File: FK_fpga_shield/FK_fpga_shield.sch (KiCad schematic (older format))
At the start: 137 parts, among them J0 USB_B_Mini, J1 molex-51382-0400-microclasp, J10 molex-51382-0400-microclasp, J11 molex-51382-0400-microclasp, J12 molex-51382-0400-microclasp, J13 molex-51382-0400-microclasp, J14 molex-51382-0400-microclasp, J15 molex-51382-0400-microclasp, J16 molex-51382-0400-microclasp, J17 molex-51382-0400-microclasp, J18 molex-51382-0400-microclasp, J19 molex-51382-0400-microclasp, J2 molex-51382-0400-microclasp, J20 molex-51382-0400-microclasp, J21 molex-51382-0400-microclasp, J22 molex-51382-0400-microclasp, J23 molex-51382-0400-microclasp, J24 molex-51382-0400-microclasp, J25 molex-51382-0400-microclasp, J26 molex-51382-0400-microclasp, J27 molex-51382-0400-microclasp, J28 molex-51382-0400-microclasp, J29 molex-51382-0400-microclasp, J3 molex-51382-0400-microclasp, J30 molex-51382-0400-microclasp, J31 molex-51382-0400-microclasp, J32 molex-51382-0400-microclasp, J33 molex-51382-0400-microclasp, J34 molex-51382-0400-microclasp, J35 molex-51382-0400-microclasp, J4 molex-51382-0400-microclasp, J5 molex-51382-0400-microclasp, J6 molex-51382-0400-microclasp, J7 molex-51382-0400-microclasp, J8 molex-51382-0400-microclasp, J9 molex-51382-0400-microclasp, U1 FT232RL, U2 nvt2010pw, U3 nvt2010pw, U4 nvt2010pw, U5 nvt2010pw, U6 nvt2010pw, U7 nvt2010pw, U8 nvt2010pw

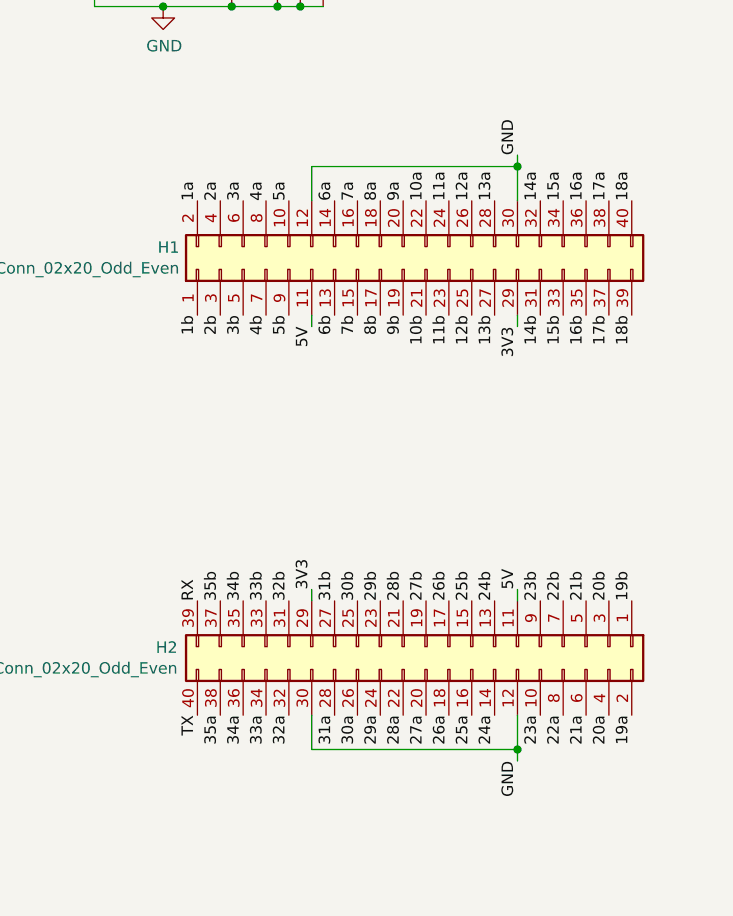
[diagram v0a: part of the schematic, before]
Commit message: levelshifter to fpga signals routed
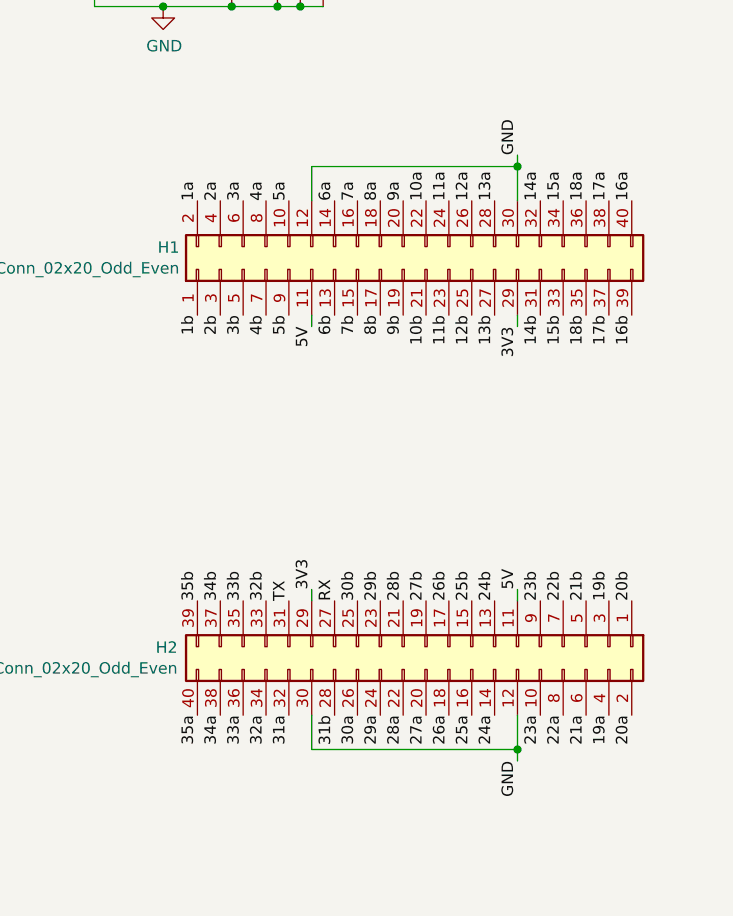
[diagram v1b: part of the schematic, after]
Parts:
- gave numbers to parts that had none: 1
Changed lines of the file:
@@
 	1    0    0    -1
 $EndComp
-Text Label 12950 6450 1    50   ~ 0
+Text Label 13550 6450 1    50   ~ 0
 RX
-Text Label 12950 6950 3    50   ~ 0
+Text Label 13350 6450 1    50   ~ 0
 TX
 Text Label 3550 2050 0    50   ~ 0
@@
 Text Label 14550 4700 1    50   ~ 0
 15a
-Text Label 14650 5200 3    50   ~ 0
+Text Label 14850 5200 3    50   ~ 0
 16b
-Text Label 14650 4700 1    50   ~ 0
+Text Label 14850 4700 1    50   ~ 0
 16a
 Text Label 14750 5200 3    50   ~ 0
@@
 Text Label 14750 4700 1    50   ~ 0
 17a
-Text Label 14850 5200 3    50   ~ 0
+Text Label 14650 5200 3    50   ~ 0
 18b
-Text Label 14850 4700 1    50   ~ 0
+Text Label 14650 4700 1    50   ~ 0
 18a
+Text Label 14750 6450 1    50   ~ 0
+19b
+Text Label 14750 6950 3    50   ~ 0
+19a
 Text Label 14850 6450 1    50   ~ 0
-19b
+20b
 Text Label 14850 6950 3    50   ~ 0
-19a
-Text Label 14750 6450 1    50   ~ 0
-20b
-Text Label 14750 6950 3    50   ~ 0
 20a
 Text Label 14650 6450 1    50   ~ 0
@@
 Text Label 14050 6450 1    50   ~ 0
 26b
-Text Label 13550 6450 1    50   ~ 0
+Text Label 13550 6950 3    50   ~ 0
 31b
-Text Label 13550 6950 3    50   ~ 0
+Text Label 13350 6950 3    50   ~ 0
 31a
-Text Label 13350 6450 1    50   ~ 0
+Text Label 13250 6450 1    50   ~ 0
 32b
-Text Label 13350 6950 3    50   ~ 0
+Text Label 13250 6950 3    50   ~ 0
 32a
-Text Label 13250 6450 1    50   ~ 0
+Text Label 13150 6450 1    50   ~ 0
 33b
-Text Label 13250 6950 3    50   ~ 0
+Text Label 13150 6950 3    50   ~ 0
 33a
-Text Label 13150 6450 1    50   ~ 0
-34b
-Text Label 13150 6950 3    50   ~ 0
-34a
-Text Label 13050 6450 1    50   ~ 0
-35b
-Text Label 13050 6950 3    50   ~ 0
-35a
 $Comp
-L Connector:Barrel_Jack J?
+L Connector:Barrel_Jack J36
 U 1 1 61D44947
 P 10300 6600
-F 0 "J?" H 10357 6925 50  0000 C CNN
+F 0 "J36" H 10357 6925 50  0000 C CNN
 F 1 "Barrel_Jack" H 10357 6834 50  0000 C CNN
 F 2 "" H 10350 6560 50  0001 C CNN
@@
 $EndComp
 $Comp
-L power:GND #PWR?
+L power:GND #PWR0112
 U 1 1 61D45B36
 P 10750 6700
-F 0 "#PWR?" H 10750 6450 50  0001 C CNN
+F 0 "#PWR0112" H 10750 6450 50  0001 C CNN
 F 1 "GND" H 10755 6527 50  0000 C CNN
 F 2 "" H 10750 6700 50  0001 C CNN
@@
 Wire Wire Line
 	10600 6500 10750 6500
+Text Label 12950 6950 3    50   ~ 0
+35a
+Text Label 13050 6950 3    50   ~ 0
+34a
+Text Label 12950 6450 1    50   ~ 0
+35b
+Text Label 13050 6450 1    50   ~ 0
+34b
 $EndSCHEMATC

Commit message: wip routing (usb done (?))
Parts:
- added C12, C13: dnp, Capacitor_SMD:C_0805_2012Metric_Pad1.15x1.40mm_HandSolder, symbol Device:C_Small
- added Y1: DNP_(12MHz), Crystal:Crystal_SMD_HC49-SD, symbol Device:Crystal
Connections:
- wire segments 541 -> 552
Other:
- note added: "External oscillator not reqired\nper datasheet when 5V powered.\nFootprint added anyway just in case."
- note removed: "External oscillator not reqired\nper datasheet when 5V powered.\n"
- moved on the sheet: C1, C2, C3, C4, J0, R1, R2, U1

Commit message: decouple 3V3 references just in case
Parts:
- removed J36: Barrel_Jack, symbol Connector:Barrel_Jack
- added C? (x7): 100n, Capacitor_SMD:C_0805_2012Metric_Pad1.15x1.40mm_HandSolder, symbol Device:C_Small
- added J36: Barrel_Jack_MountingPin, Connector_BarrelJack:BarrelJack_CUI_PJ-063AH_Horizontal, symbol Connector:Barrel_Jack_MountingPin
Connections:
- wire segments 552 -> 573
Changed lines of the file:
@@
 	1    0    0    -1
 $EndComp
-Wire Wire Line
-	3600 10450 3450 10450
 Text Label 3600 10550 3    50   ~ 0
 3V3
@@
 33a
 $Comp
-L Connector:Barrel_Jack J36
-U 1 1 61D44947
-P 10300 6600
-F 0 "J36" H 10357 6925 50  0000 C CNN
-F 1 "Barrel_Jack" H 10357 6834 50  0000 C CNN
-F 2 "" H 10350 6560 50  0001 C CNN
-F 3 "~" H 10350 6560 50  0001 C CNN
-	1    10300 6600
-	1    0    0    -1
-$EndComp
-$Comp
 L power:GND #PWR0112
 U 1 1 61D45B36
-P 10750 6700
-F 0 "#PWR0112" H 10750 6450 50  0001 C CNN
-F 1 "GND" H 10755 6527 50  0000 C CNN
-F 2 "" H 10750 6700 50  0001 C CNN
-F 3 "" H 10750 6700 50  0001 C CNN
-	1    10750 6700
-	1    0    0    -1
-$EndComp
-Wire Wire Line
-	10600 6700 10750 6700
-Text Label 10750 6500 0    50   ~ 0
+P 9400 7000
+F 0 "#PWR0112" H 9400 6750 50  0001 C CNN
+F 1 "GND" H 9405 6827 50  0000 C CNN
+F 2 "" H 9400 7000 50  0001 C CNN
+F 3 "" H 9400 7000 50  0001 C CNN
+	1    9400 7000
+	1    0    0    -1
+$EndComp
+Text Label 9600 6300 0    50   ~ 0
 5V
 Wire Wire Line
-	10600 6500 10750 6500
+	9500 6500 9600 6500
 Text Label 12950 6950 3    50   ~ 0
 35a
@@
 Wire Wire Line
 	10550 3200 10750 3200
+Wire Wire Line
+	9600 6500 9600 6300
+Wire Wire Line
+	9500 6700 9600 6700
+Wire Wire Line
+	9600 6500 10650 6500
+Connection ~ 9600 6500
+Wire Wire Line
+	9600 6700 10650 6700
+Connection ~ 9600 6700
+$Comp
+L Connector:Barrel_Jack_MountingPin J36
+U 1 1 60468A7D
+P 9200 6600
+F 0 "J36" H 9257 6917 50  0000 C CNN
+F 1 "Barrel_Jack_MountingPin" H 9257 6826 50  0000 C CNN
+F 2 "Connector_BarrelJack:BarrelJack_CUI_PJ-063AH_Horizontal" H 9250 6560 50  0001 C CNN
+F 3 "~" H 9250 6560 50  0001 C CNN
+	1    9200 6600
+	1    0    0    -1
+$EndComp
+Wire Wire Line
+	9200 6900 9400 6900
+Wire Wire Line
+	9400 6900 9400 7000
+Wire Wire Line
+	9400 6900 9600 6900
+Wire Wire Line
+	9600 6700 9600 6900
+Connection ~ 9400 6900
+$Comp
+L Device:C_Small C?
+U 1 1 6051B8E6
+P 8000 4350
+F 0 "C?" H 7800 4400 50  0000 L CNN
+F 1 "100n" H 7650 4300 50  0000 L CNN
+F 2 "Capacitor_SMD:C_0805_2012Metric_Pad1.15x1.40mm_HandSolder" H 8000 4350 50  0001 C CNN
+F 3 "~" H 8000 4350 50  0001 C CNN
+	1    8000 4350
+	0    -1   -1   0
+$EndComp
+Connection ~ 7900 4350
+Wire Wire Line
+	8100 4350 8100 4650
+Wire Wire Line
+	8100 4650 7750 4650
+$Comp
+L Device:C_Small C?
+U 1 1 60572E7D
+P 8000 2250
+F 0 "C?" H 7800 2300 50  0000 L CNN
+F 1 "100n" H 7650 2200 50  0000 L CNN
+F 2 "Capacitor_SMD:C_0805_2012Metric_Pad1.15x1.40mm_HandSolder" H 8000 2250 50  0001 C CNN
+F 3 "~" H 8000 2250 50  0001 C CNN
+	1    8000 2250
+	0    1    1    0
+$EndComp
+Connection ~ 7900 2250
+Wire Wire Line
+	8100 2250 8100 2550
+Wire Wire Line
+	8100 2550 7750 2550
+$Comp
+L Device:C_Small C?
+U 1 1 605CB24D
+P 3700 2250
+F 0 "C?" H 3500 2300 50  0000 L CNN
+F 1 "100n" H 3350 2200 50  0000 L CNN
+F 2 "Capacitor_SMD:C_0805_2012Metric_Pad1.15x1.40mm_HandSolder" H 3700 2250 50  0001 C CNN
+F 3 "~" H 3700 2250 50  0001 C CNN
+	1    3700 2250
+	0    1    1    0
+$EndComp
+Connection ~ 3600 2250
+Wire Wire Line
+	3800 2250 3800 2550
+Wire Wire Line
+	3800 2550 3450 2550
+$Comp
+L Device:C_Small C?
+U 1 1 6062316B
+P 3700 4300
+F 0 "C?" H 3500 4350 50  0000 L CNN
+F 1 "100n" H 3350 4250 50  0000 L CNN
+F 2 "Capacitor_SMD:C_0805_2012Metric_Pad1.15x1.40mm_HandSolder" H 3700 4300 50  0001 C CNN
+F 3 "~" H 3700 4300 50  0001 C CNN
+	1    3700 4300
+	0    1    1    0
+$EndComp
+Connection ~ 3600 4300
+Wire Wire Line
+	3800 4300 3800 4600
+Wire Wire Line
+	3800 4600 3450 4600
+$Comp
+L Device:C_Small C?
+U 1 1 6067B91E
+P 3700 6350
+F 0 "C?" H 3500 6400 50  0000 L CNN
+F 1 "100n" H 3350 6300 50  0000 L CNN
+F 2 "Capacitor_SMD:C_0805_2012Metric_Pad1.15x1.40mm_HandSolder" H 3700 6350 50  0001 C CNN
+F 3 "~" H 3700 6350 50  0001 C CNN
+	1    3700 6350
+	0    1    1    0
+$EndComp
+Connection ~ 3600 6350
+Wire Wire Line
+	3800 6350 3800 6650
+Wire Wire Line
+	3800 6650 3450 6650
+$Comp
+L Device:C_Small C?
+U 1 1 606D48EA
+P 3700 8400
+F 0 "C?" H 3500 8450 50  0000 L CNN
+F 1 "100n" H 3350 8350 50  0000 L CNN
+F 2 "Capacitor_SMD:C_0805_2012Metric_Pad1.15x1.40mm_HandSolder" H 3700 8400 50  0001 C CNN
+F 3 "~" H 3700 8400 50  0001 C CNN
+	1    3700 8400
+	0    1    1    0
+$EndComp
+Connection ~ 3600 8400
+Wire Wire Line
+	3800 8400 3800 8700
+Wire Wire Line
+	3800 8700 3450 8700
+Wire Wire Line
+	3600 10450 3450 10450
+$Comp
+L Device:C_Small C?
+U 1 1 6072F97B
+P 3700 10450
+F 0 "C?" H 3500 10500 50  0000 L CNN
+F 1 "100n" H 3350 10400 50  0000 L CNN
+F 2 "Capacitor_SMD:C_0805_2012Metric_Pad1.15x1.40mm_HandSolder" H 3700 10450 50  0001 C CNN
+F 3 "~" H 3700 10450 50  0001 C CNN
+	1    3700 10450
+	0    1    1    0
+$EndComp
+Connection ~ 3600 10450
+Wire Wire Line
+	3800 10450 3800 10750
+Wire Wire Line
+	3800 10750 3450 10750
 $EndSCHEMATC
